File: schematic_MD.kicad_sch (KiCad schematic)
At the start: 7 parts, among them SW1 SW_MEC_5E, U1 STM32F303K8Tx, Y1 Crystal

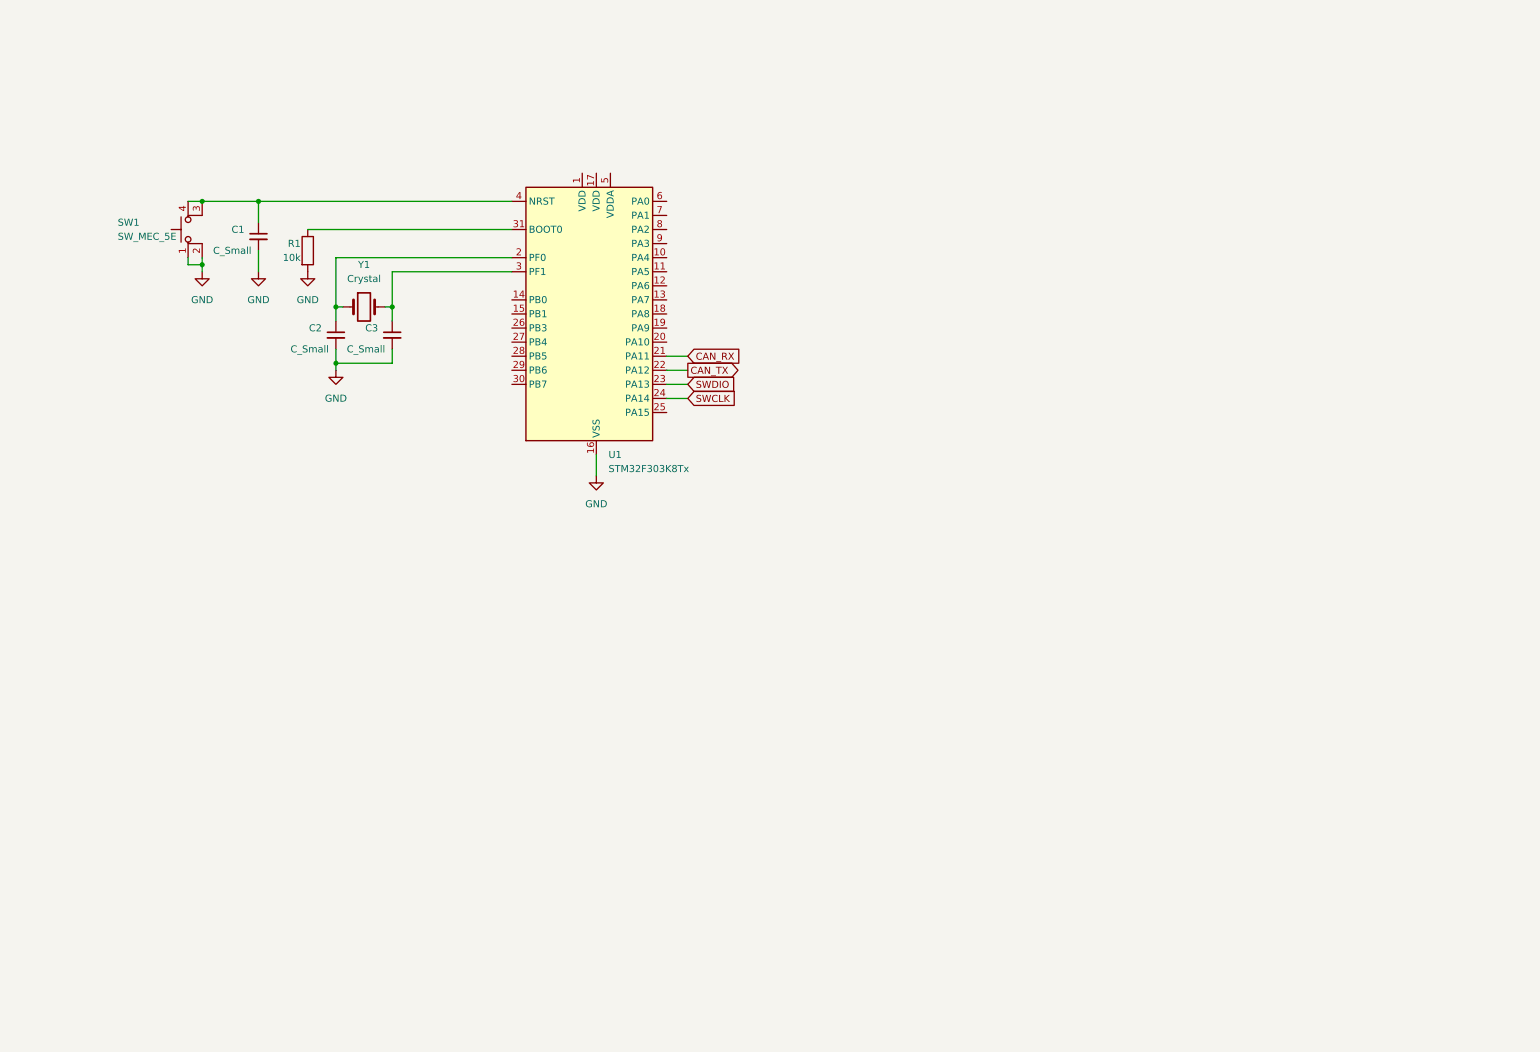
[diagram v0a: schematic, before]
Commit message: schematic update
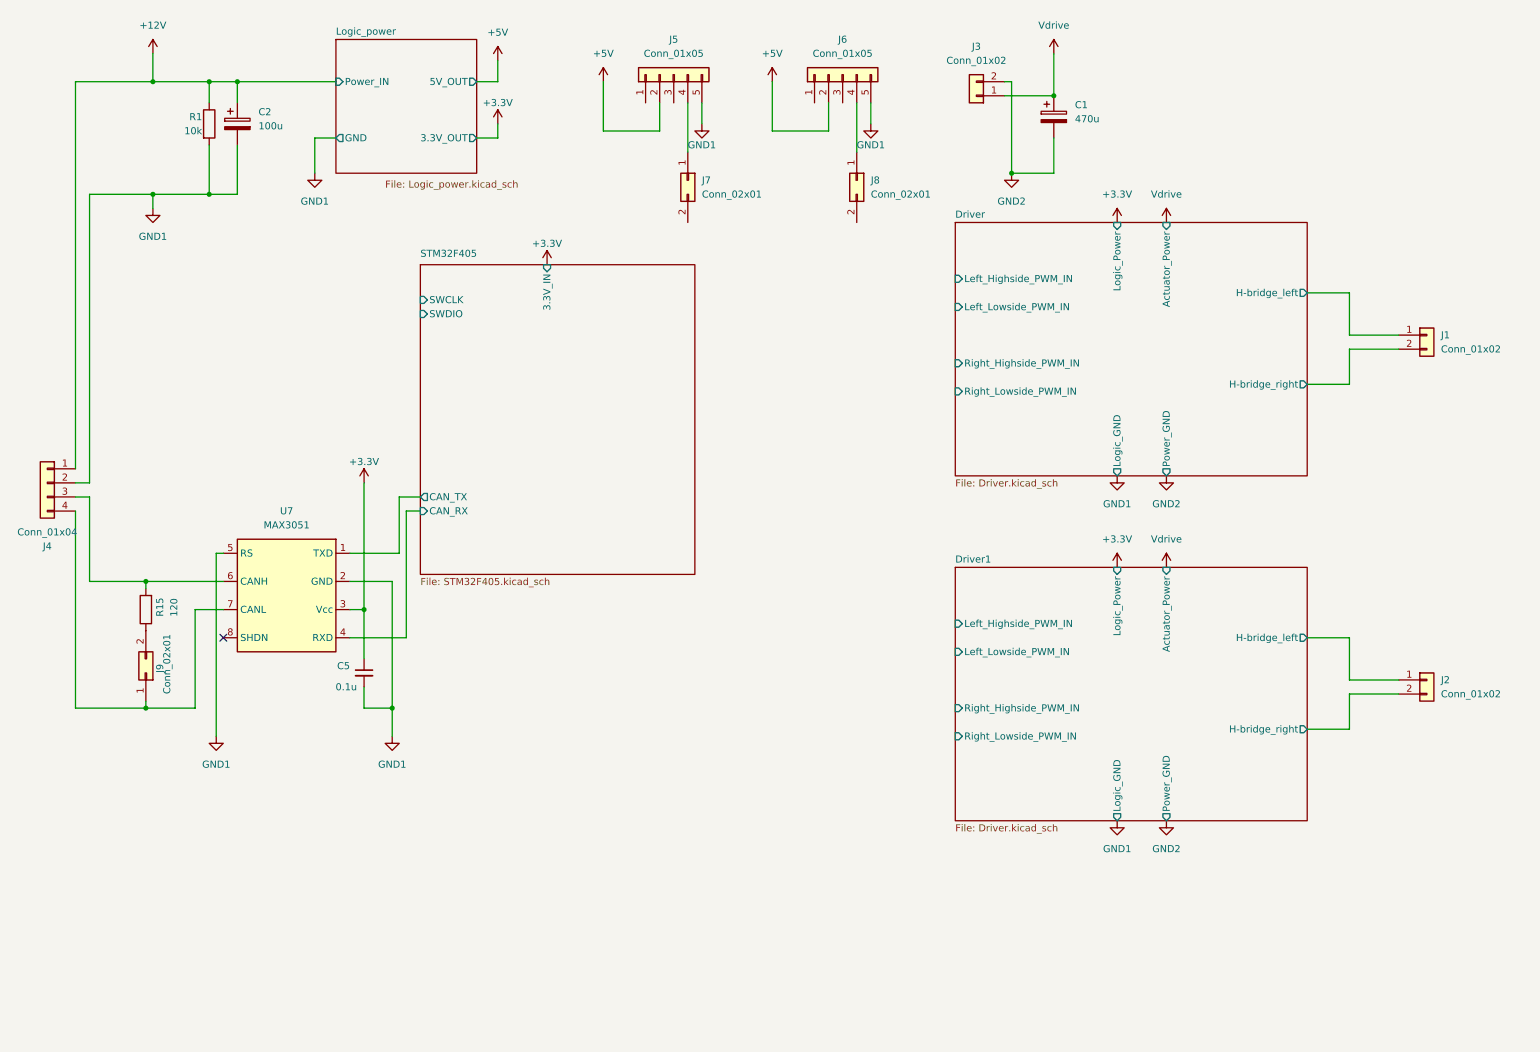
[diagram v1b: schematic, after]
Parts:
- removed C1, C2, C3: C_Small, symbol Device:C_Small
- removed SW1: SW_MEC_5E, symbol Switch:SW_MEC_5E
- removed U1: STM32F303K8Tx, Package_QFP:LQFP-32_7x7mm_P0.8mm, symbol MCU_ST_STM32F3:STM32F303K8Tx
- removed Y1: Crystal, symbol Device:Crystal
- added C1: 470u, symbol Device:C_Polarized
- added C2: 100u, symbol Device:C_Polarized
- added C5: 0.1u, symbol Device:C_Small
- added J1, J2, J3: Conn_01x02, symbol Connector_Generic:Conn_01x02
- added J4: Conn_01x04, Connector_JST:JST_XA_B04B-XASK-1_1x04_P2.50mm_Vertical, symbol Connector_Generic:Conn_01x04
- added J5, J6: Conn_01x05, Connector_JST:JST_XA_B05B-XASK-1_1x05_P2.50mm_Vertical, symbol Connector_Generic:Conn_01x05
- added J7, J8, J9: Conn_02x01, Connector_PinHeader_2.54mm:PinHeader_1x02_P2.54mm_Vertical, symbol Connector_Generic:Conn_02x01
- added R15: 120, symbol Device:R
- added U7: MAX3051, Package_TO_SOT_SMD:SOT-23-8_Handsoldering, symbol RDC_generic:MAX3051
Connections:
- net +12V: now reaches R1.1
- net +12V: now also C2.1, J4.1 (Pin_1)
- net GND renamed GND1
- net GND1: now also C2.2, C5.2, J4.2 (Pin_2), J5.5 (Pin_5), J6.5 (Pin_5), U7.2 (GND), U7.5 (RS)
- new net: J6.4 (Pin_4), J8.1 (Pin_1)
- new net: J4.3 (Pin_3), R15.2, U7.6 (CANH)
- new net: J4.4 (Pin_4), J9.1 (Pin_1), U7.7 (CANL)
- new net: J9.2 (Pin_2), R15.1
- new net: J5.4 (Pin_4), J7.1 (Pin_1)
- new net +3.3V: C5.1, U7.3 (Vcc)
- new net +5V: J5.2 (Pin_2), J6.2 (Pin_2)
- new net Driver/H-bridge_left: J1.1 (Pin_1)
- new net Driver/H-bridge_right: J1.2 (Pin_2)
- new net Driver1/H-bridge_left: J2.1 (Pin_1)
- new net Driver1/H-bridge_right: J2.2 (Pin_2)
- new net GND2: C1.2, J3.2 (Pin_2)
- new net STM32F405/CAN_RX: U7.4 (RXD)
- new net STM32F405/CAN_TX: U7.1 (TXD)
- new net Vdrive: C1.1, J3.1 (Pin_1)
- no-connect marks 0 -> 1
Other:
- added sheet Driver (Driver.kicad_sch)
- added sheet Driver1 (Driver.kicad_sch)
- added sheet Logic_power (Logic_power.kicad_sch)
- added sheet STM32F405 (STM32F405.kicad_sch)

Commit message: update Driver circuit
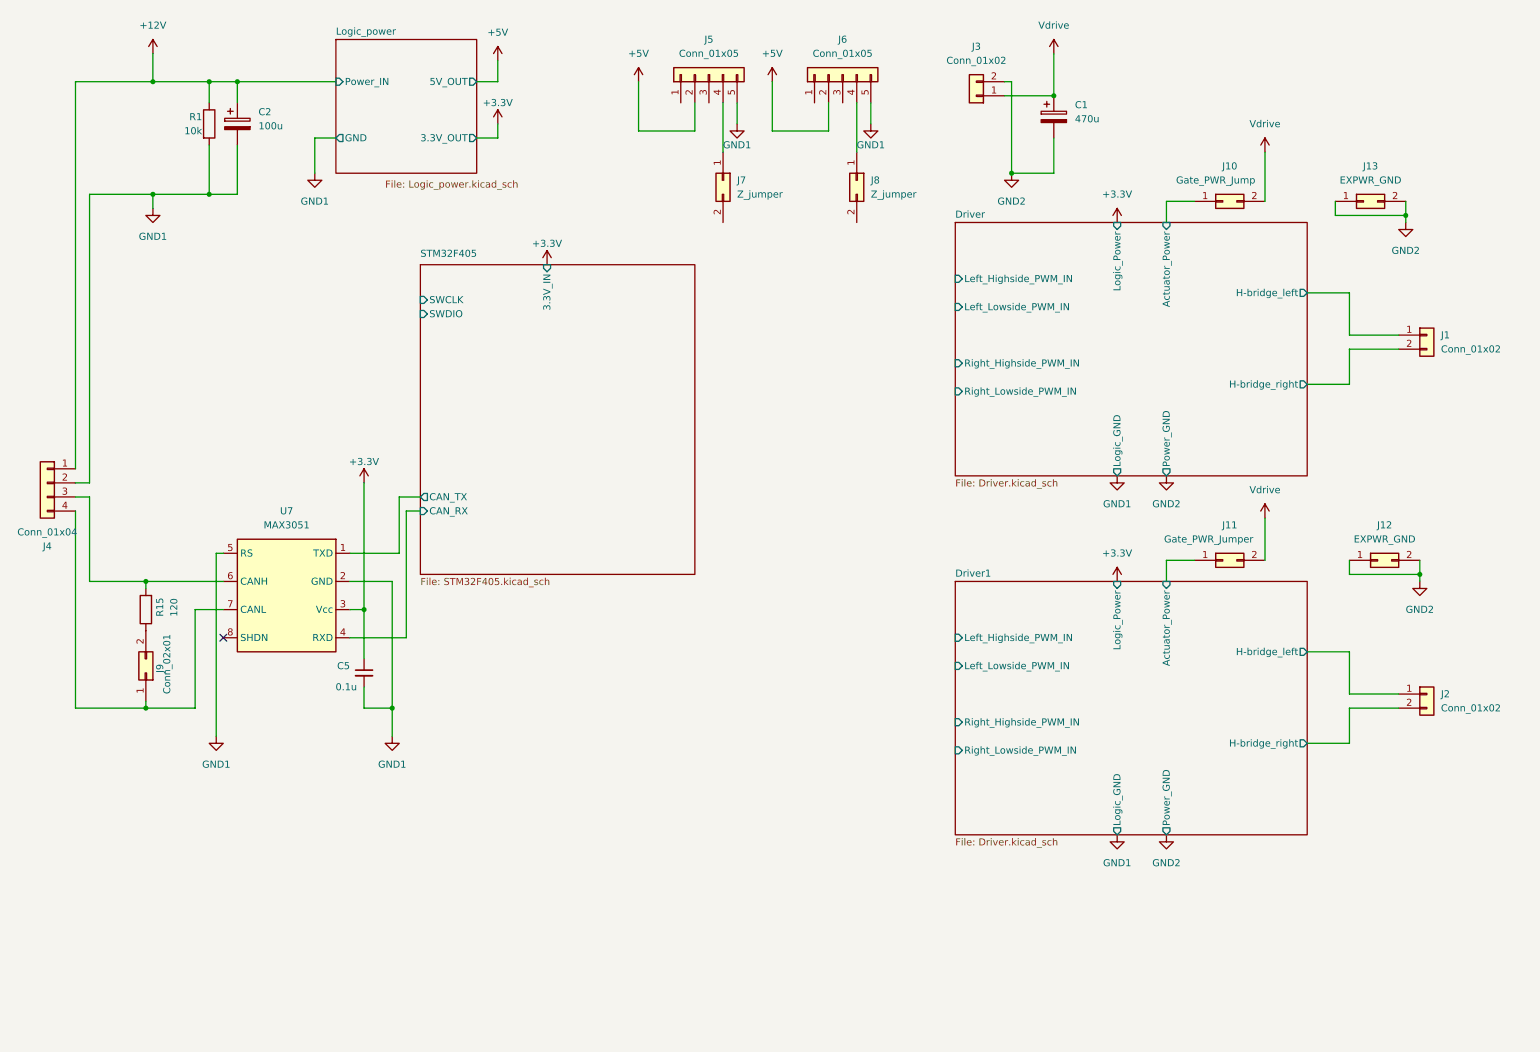
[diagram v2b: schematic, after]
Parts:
- added J10: Gate_PWR_Jump, Connector_PinHeader_2.54mm:PinHeader_1x02_P2.54mm_Vertical, symbol Connector_Generic:Conn_02x01
- added J11: Gate_PWR_Jumper, Connector_PinHeader_2.54mm:PinHeader_1x02_P2.54mm_Vertical, symbol Connector_Generic:Conn_02x01
- added J12, J13: EXPWR_GND, Connector_PinHeader_2.54mm:PinHeader_1x02_P2.54mm_Vertical, symbol Connector_Generic:Conn_02x01
- J7, J8: value Conn_02x01 -> Z_jumper
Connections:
- net GND2: now also J12.1 (Pin_1), J12.2 (Pin_2), J13.1 (Pin_1), J13.2 (Pin_2)
- net Vdrive: now also J10.2 (Pin_2), J11.2 (Pin_2)
- new net Driver/Actuator_Power: J10.1 (Pin_1)
- new net Driver1/Actuator_Power: J11.1 (Pin_1)
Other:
- moved on the sheet: J2, J5, J7

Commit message: update parts list
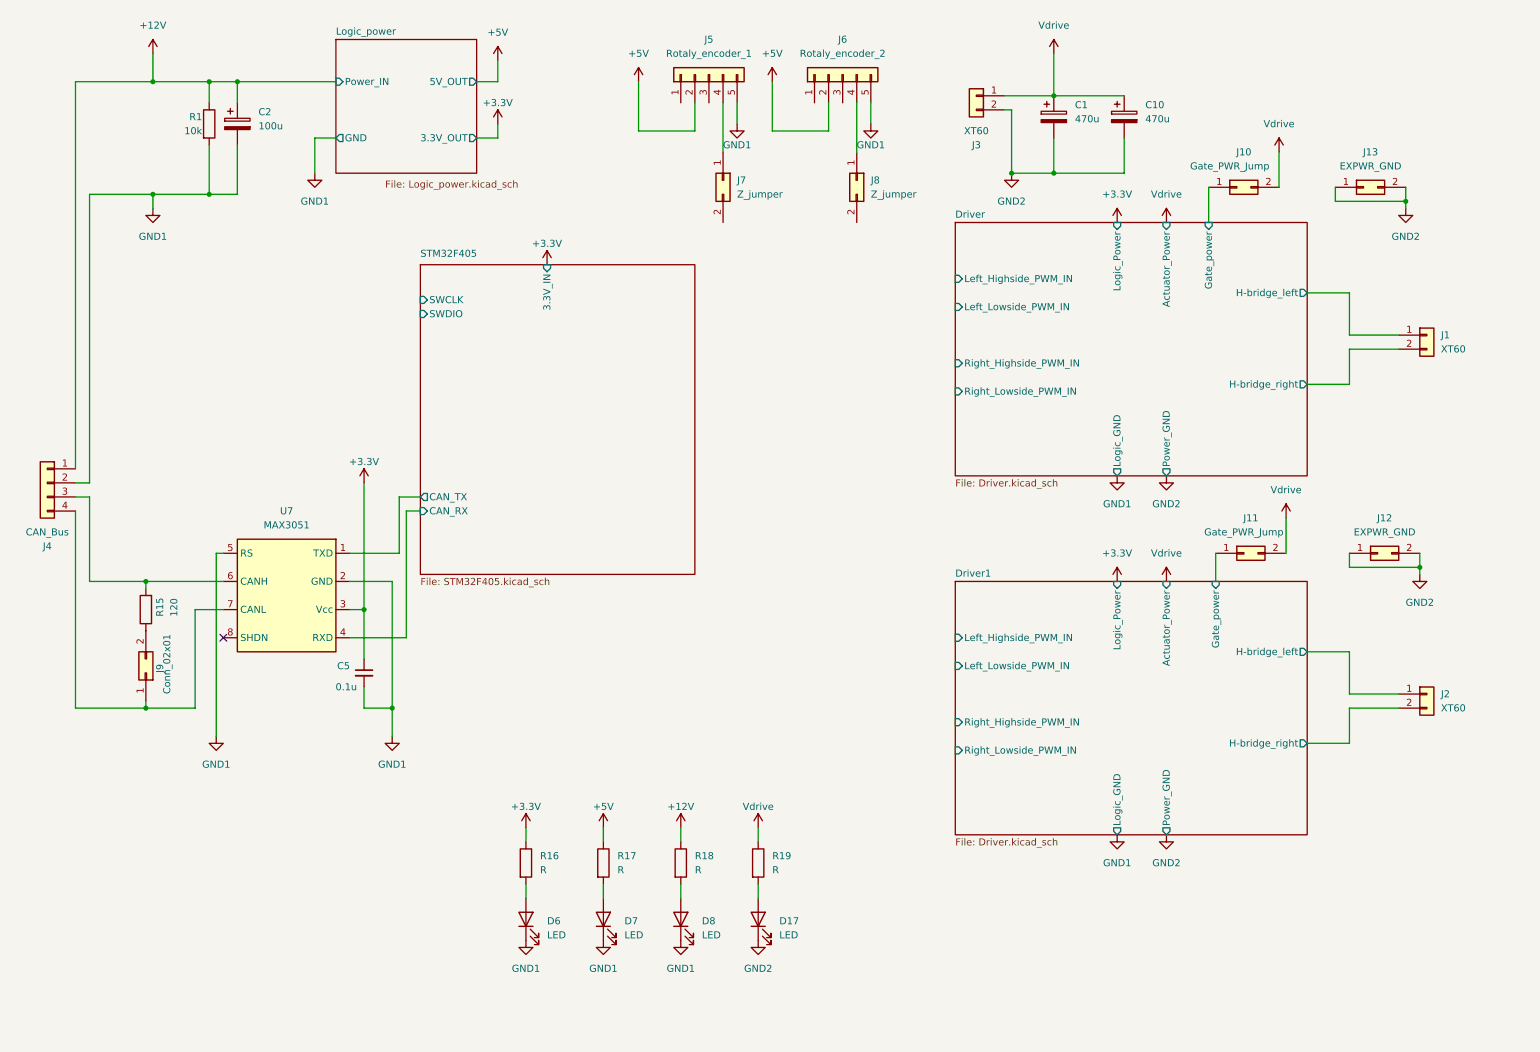
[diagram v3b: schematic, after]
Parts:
- added C10: 470u, symbol Device:C_Polarized
- added D17, D6, D7, D8: LED, symbol Device:LED
- added R16, R17, R18, R19: R, symbol Device:R
- J1, J2, J3: value Conn_01x02 -> XT60
- J11: value Gate_PWR_Jumper -> Gate_PWR_Jump
- J4: value Conn_01x04 -> CAN_Bus
- J5: value Conn_01x05 -> Rotaly_encoder_1
- J6: value Conn_01x05 -> Rotaly_encoder_2
- R1: footprint (none) -> Resistor_SMD:R_1206_3216Metric_Pad1.30x1.75mm_HandSolder
- R15: footprint (none) -> Resistor_SMD:R_0603_1608Metric_Pad0.98x0.95mm_HandSolder
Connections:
- net +12V: now also R18.1
- net +3.3V: now also R16.1
- net +5V: now also R17.1
- net GND1: now also D6.1 (K), D7.1 (K), D8.1 (K)
- net GND2: now also C10.2, D17.1 (K)
- net Vdrive: now also C10.1, R19.1
- net Driver/Actuator_Power renamed Driver/Gate_power
- net Driver1/Actuator_Power renamed Driver1/Gate_power
- new net: D6.2 (A), R16.2
- new net: D7.2 (A), R17.2
- new net: D17.2 (A), R19.2
- new net: D8.2 (A), R18.2
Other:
- sheet Driver ports: added Gate_power; removed none
- sheet Driver1 ports: added Gate_power; removed none
- moved on the sheet: J12, J13, J3

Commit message: add footprint
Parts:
- added C11, C12: 330u, Capacitor_THT:CP_Radial_D10.0mm_P5.00mm, symbol Device:C_Polarized
- C1, C10: value 470u -> 330u; footprint (none) -> Capacitor_THT:CP_Radial_D10.0mm_P5.00mm
- C2: footprint (none) -> Capacitor_THT:CP_Radial_D6.3mm_P2.50mm
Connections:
- net GND2: now also C11.2, C12.2
- net Vdrive: now also C11.1, C12.1
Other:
- moved on the sheet: C1, C10, J3

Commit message: pattern update
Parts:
- D17, D6, D7, D8: footprint (none) -> LED_SMD:LED_0603_1608Metric_Pad1.05x0.95mm_HandSolder
- J1, J2, J3: footprint (none) -> RDC_footprint:XT60
- R16: value R -> 320
- R17: value R -> 680
- R18: value R -> 2k
- R19: value R -> 3.6k
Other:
- note added: "V_{F} = 1.7V @ I_{F} = 5mA R_{LED} = (V - V_{F}) ÷ I_{F} MAX loss 0.09W @ Vdrive = 24V"
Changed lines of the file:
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@@
     (stroke (width 0) (type default))
+  )
+  (text "V_{F} = 1.7V @ I_{F} = 5mA\n\nR_{LED} = (V - V_{F}) ÷ I_{F}\n\nMAX loss 0.09W @ Vdrive = 24V"
+    (at 104.14 196.85 0)
+    (effects (font (size 1.27 1.27)) (justify left bottom))
   )
   (symbol (lib_id "Device:C_Polarized") (at 217.17 24.13 0) (unit 1)
@@
       (effects (font (size 1.27 1.27)) (justify right))
     )
-    (property "Footprint" "" (at 106.68 175.26 0)
+    (property "Footprint" "LED_SMD:LED_0603_1608Metric_Pad1.05x0.95mm_HandSolder" (at 106.68 175.26 0)
       (effects (font (size 1.27 1.27)) hide)
     )
@@
       (effects (font (size 1.27 1.27)) (justify left))
     )
-    (property "Footprint" "" (at 269.24 69.85 0)
+    (property "Footprint" "RDC_footprint:XT60" (at 269.24 69.85 0)
       (effects (font (size 1.27 1.27)) hide)
     )
@@
       (effects (font (size 1.27 1.27)) (justify left))
     )
-    (property "Value" "R" (at 123.19 166.37 0)
+    (property "Value" "680" (at 123.19 166.37 0)
       (effects (font (size 1.27 1.27)) (justify left))
     )
@@
       (effects (font (size 1.27 1.27)) (justify right))
     )
-    (property "Footprint" "" (at 120.65 175.26 0)
+    (property "Footprint" "LED_SMD:LED_0603_1608Metric_Pad1.05x0.95mm_HandSolder" (at 120.65 175.26 0)
       (effects (font (size 1.27 1.27)) hide)
     )
@@
       (effects (font (size 1.27 1.27)) (justify left))
     )
-    (property "Footprint" "" (at 269.24 134.62 0)
+    (property "Footprint" "RDC_footprint:XT60" (at 269.24 134.62 0)
       (effects (font (size 1.27 1.27)) hide)
     )
@@
       (effects (font (size 1.27 1.27)) (justify right))
     )
-    (property "Footprint" "" (at 148.59 175.26 0)
+    (property "Footprint" "LED_SMD:LED_0603_1608Metric_Pad1.05x0.95mm_HandSolder" (at 148.59 175.26 0)
       (effects (font (size 1.27 1.27)) hide)
     )
@@
       (effects (font (size 1.27 1.27)) (justify left))
     )
-    (property "Value" "R" (at 137.16 166.37 0)
+    (property "Value" "2k" (at 137.16 166.37 0)
       (effects (font (size 1.27 1.27)) (justify left))
     )
@@
       (effects (font (size 1.27 1.27)))
     )
-    (property "Footprint" "" (at 180.34 17.78 0)
+    (property "Footprint" "RDC_footprint:XT60" (at 180.34 17.78 0)
       (effects (font (size 1.27 1.27)) hide)
     )
@@
       (effects (font (size 1.27 1.27)) (justify left))
     )
-    (property "Value" "R" (at 151.13 166.37 0)
+    (property "Value" "3.6k" (at 151.13 166.37 0)
       (effects (font (size 1.27 1.27)) (justify left))
     )
@@
       (effects (font (size 1.27 1.27)) (justify left))
     )
-    (property "Value" "R" (at 109.22 166.37 0)
+    (property "Value" "320" (at 109.22 166.37 0)
       (effects (font (size 1.27 1.27)) (justify left))
     )
@@
       (effects (font (size 1.27 1.27)) (justify right))
     )
-    (property "Footprint" "" (at 134.62 175.26 0)
-      (effects (font (size 1.27 1.27)) hide)
-    )
+    (property "Footprint" "LED_SMD:LED_0603_1608Metric_Pad1.05x0.95mm_HandSolder" (at 134.62 175.26 0)
+      (effects (font (size 1.27 1.27)) hide)
+    )
